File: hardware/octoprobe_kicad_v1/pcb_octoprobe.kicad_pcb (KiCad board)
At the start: 2 copper layers, 100 x 160 mm, 624 parts, among them J1001 Conn_01x02_Socket, J1002 Conn_01x02_Socket, J1003 Conn_01x02_Pin, J101 Conn_01x20, J102 Conn_01x20, J103 Conn_01x20, J201 USB_C_Receptacle_USB2.0, J301 Conn_01x02_Socket, J302 Conn_01x02_Socket, J303 Conn_01x02_Pin, J401 Conn_01x02_Socket, J402 Conn_01x02_Socket, J403 Conn_01x02_Pin, J501 Conn_01x02_Socket, J502 Conn_01x02_Socket, J503 Conn_01x02_Pin, J601 Conn_01x02_Socket, J602 Conn_01x02_Socket, J603 Conn_01x02_Pin, J701 Conn_01x02_Socket, J702 Conn_01x02_Socket, J703 Conn_01x02_Pin, J801 Conn_01x02_Socket, J802 Conn_01x02_Socket, J803 Conn_01x02_Pin, J901 Conn_01x02_Socket, J902 Conn_01x02_Socket, J903 Conn_01x02_Pin, SW201 SW_MEC_5E, U1001 GAQY221S, U201 RP2040, U202 AMS1117-3.3, U203 W25Q128JVS, U301 GAQY221S, U401 GAQY221S, U701 GAQY221S, U901 GAQY221S, Y201 Crystal_GND24_Small

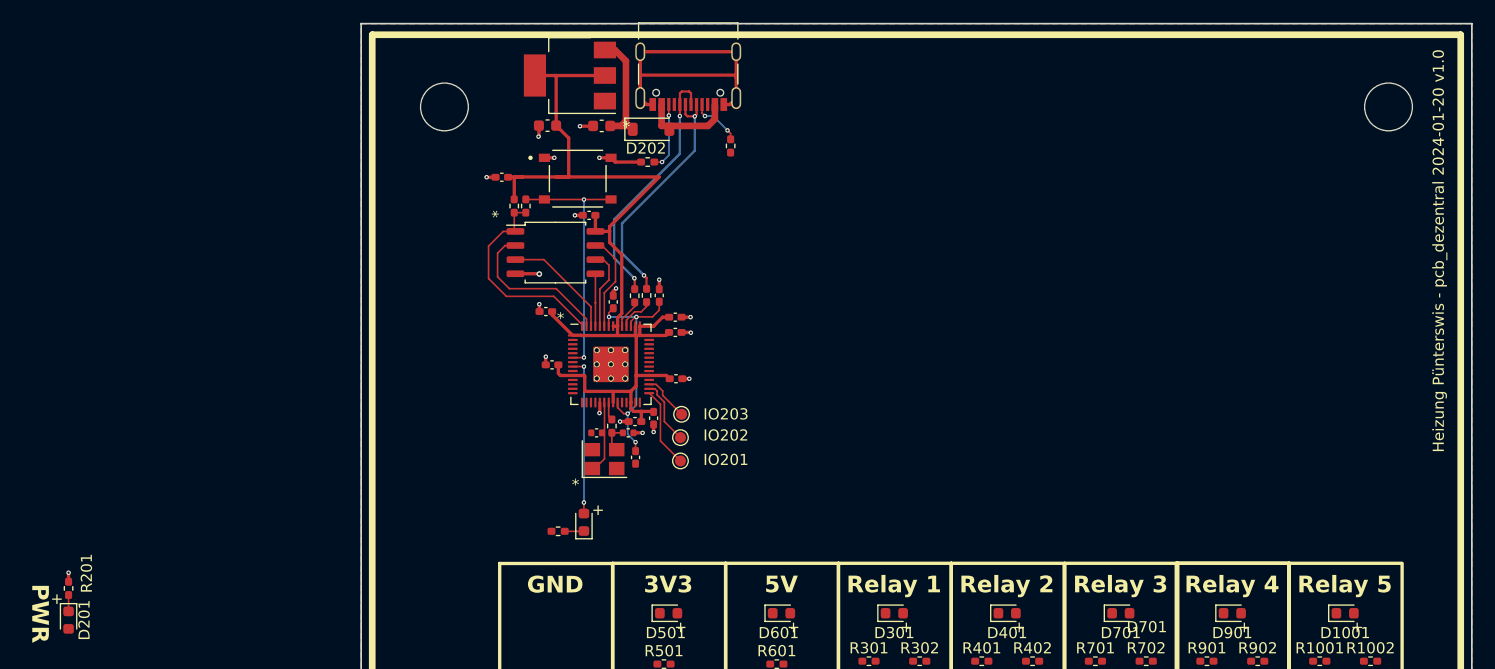
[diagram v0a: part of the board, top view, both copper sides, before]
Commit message: update sheet names
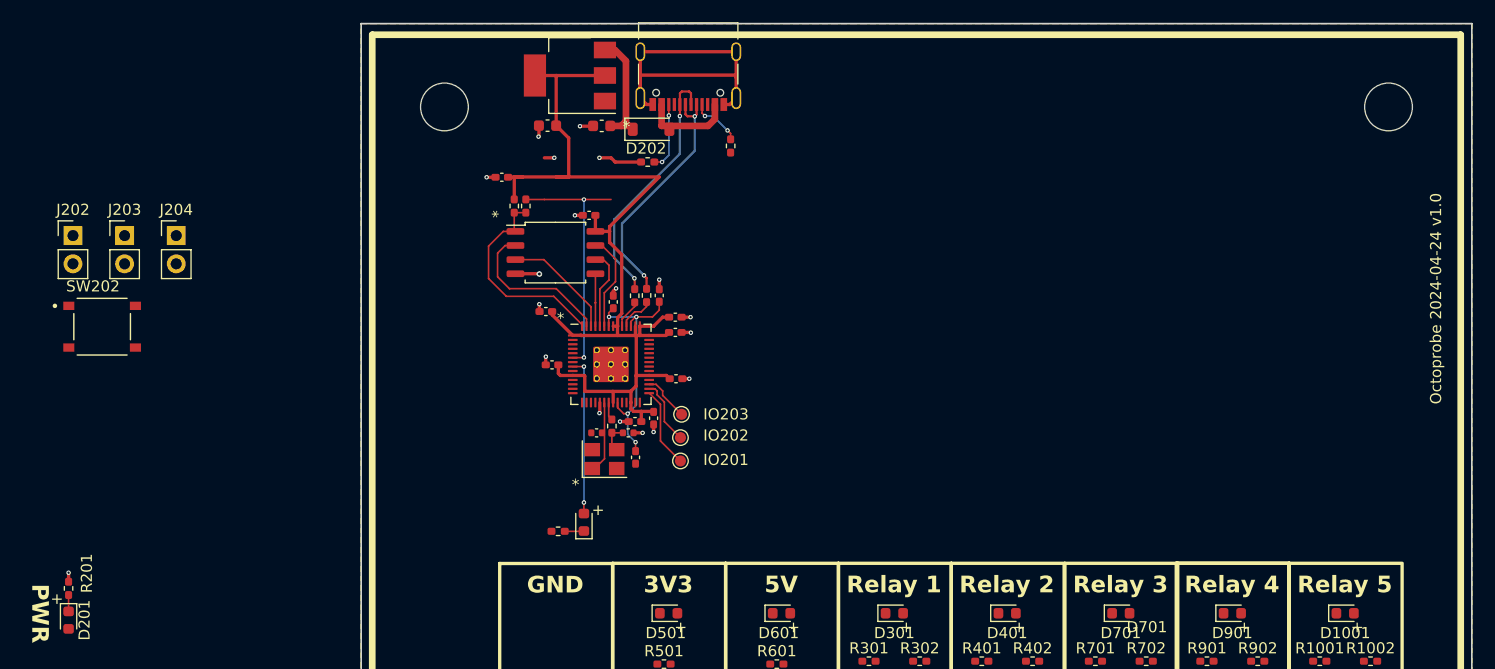
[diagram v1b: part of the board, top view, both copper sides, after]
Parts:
- removed SW201: SW_MEC_5E, 00_project_library:SW_TS-1187A-B-A-B
- added J202: BOOT cap enable, Connector_PinHeader_2.54mm:PinHeader_1x02_P2.54mm_Vertical, F.Cu at (48.1, 51.6)
- added J203: BOOT Button, Connector_PinHeader_2.54mm:PinHeader_1x02_P2.54mm_Vertical, F.Cu at (52.7, 51.6)
- added J204: BOOT cap 2, Connector_PinHeader_2.54mm:PinHeader_1x02_P2.54mm_Vertical, F.Cu at (57.4, 51.6)
- added SW202: RESET, 00_project_library:SW_TS-1187A-B-A-B, F.Cu at (50.7, 59.8)
- R1002, R302, R402, R702, R902: value 10K -> 4k2
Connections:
- U201 pad 26: +3V3 -> Net-(U201-RUN)

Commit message: Breakout Board
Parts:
- removed the REF** at (79.1, 129.0)
- removed REF**1, REF**10, REF**100, REF**101, REF**102, REF**103, REF**104, REF**105, REF**106, REF**107, REF**108, REF**109, REF**11, REF**110, REF**111, REF**112, REF**113, REF**114, REF**115, REF**116, REF**117, REF**118, REF**119, REF**12, REF**120, REF**121, REF**122, REF**123, REF**124, REF**125, REF**126, REF**127, REF**128, REF**129, REF**13, REF**130, REF**131, REF**132, REF**133, REF**134, REF**135, REF**136, REF**137, REF**138, REF**139, REF**14, REF**140, REF**141, REF**142, REF**143, REF**144, REF**145, REF**146, REF**147, REF**148, REF**149, REF**15, REF**150, REF**151, REF**152, REF**153, REF**154, REF**155, REF**156, REF**157, REF**158, REF**159, REF**16, REF**160, REF**161, REF**162, REF**163, REF**164, REF**165, REF**166, REF**167, REF**168, REF**169, REF**17, REF**170, REF**171, REF**172, REF**173, REF**174, REF**175, REF**176, REF**177, REF**178, REF**179, REF**18, REF**180, REF**181, REF**182, REF**183, REF**184, REF**185, REF**186, REF**187, REF**188, REF**189, REF**19, REF**190, REF**191, REF**192, REF**193, REF**194, REF**195, REF**196, REF**197, REF**198, REF**199, REF**2, REF**20, REF**200, REF**201, REF**202, REF**203, REF**204, REF**205, REF**206, REF**207, REF**208, REF**209, REF**21, REF**210, REF**211, REF**212, REF**213, REF**214, REF**215, REF**216, REF**217, REF**218, REF**219, REF**22, REF**220, REF**221, REF**222, REF**223, REF**224, REF**225, REF**226, REF**227, REF**228, REF**229, REF**23, REF**230, REF**231, REF**232, REF**233, REF**234, REF**235, REF**236, REF**237, REF**238, REF**239, REF**24, REF**240, REF**241, REF**242, REF**243, REF**244, REF**245, REF**246, REF**247, REF**248, REF**249, REF**25, REF**250, REF**251, REF**252, REF**253, REF**254, REF**255, REF**256, REF**257, REF**258, REF**259, REF**26, REF**260, REF**261, REF**262, REF**263, REF**264, REF**265, REF**266, REF**267, REF**268, REF**269, REF**27, REF**270, REF**271, REF**272, REF**273, REF**274, REF**275, REF**276, REF**277, REF**278, REF**279, REF**28, REF**280, REF**281, REF**282, REF**283, REF**284, REF**285, REF**286, REF**287, REF**288, REF**289, REF**29, REF**290, REF**291, REF**292, REF**293, REF**294, REF**295, REF**296, REF**297, REF**298, REF**299, REF**3, REF**30, REF**300, REF**301, REF**302, REF**303, REF**304, REF**305, REF**306, REF**307, REF**308, REF**309, REF**31, REF**310, REF**311, REF**312, REF**313, REF**314, REF**315, REF**316, REF**317, REF**318, REF**319, REF**32, REF**320, REF**321, REF**322, REF**323, REF**324, REF**325, REF**326, REF**327, REF**328, REF**329, REF**33, REF**330, REF**331, REF**332, REF**333, REF**334, REF**335, REF**336, REF**337, REF**338, REF**339, REF**34, REF**340, REF**341, REF**342, REF**343, REF**344, REF**345, REF**346, REF**347, REF**348, REF**349, REF**35, REF**350, REF**351, REF**352, REF**353, REF**354, REF**355, REF**356, REF**357, REF**358, REF**359, REF**36, REF**360, REF**361, REF**362, REF**363, REF**364, REF**365, REF**366, REF**367, REF**368, REF**369, REF**37, REF**370, REF**371, REF**372, REF**373, REF**374, REF**375, REF**376, REF**377, REF**378, REF**379, REF**38, REF**380, REF**381, REF**382, REF**383, REF**384, REF**385, REF**386, REF**387, REF**388, REF**389, REF**39, REF**390, REF**391, REF**392, REF**393, REF**394, REF**395, REF**396, REF**397, REF**398, REF**399, REF**4, REF**40, REF**400, REF**401, REF**402, REF**403, REF**404, REF**405, REF**406, REF**407, REF**408, REF**409, REF**41, REF**410, REF**411, REF**412, REF**413, REF**414, REF**415, REF**416, REF**417, REF**418, REF**419, REF**42, REF**420, REF**421, REF**422, REF**423, REF**424, REF**425, REF**426, REF**427, REF**428, REF**429, REF**43, REF**430, REF**431, REF**432, REF**433, REF**434, REF**435, REF**436, REF**437, REF**438, REF**439, REF**44, REF**440, REF**441, REF**442, REF**443, REF**444, REF**445, REF**446, REF**447, REF**448, REF**449, REF**45, REF**450, REF**451, REF**452, REF**453, REF**454, REF**455, REF**456, REF**457, REF**458, REF**459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: TestPoint_THTPad_D2.0mm_Drill1.0mm, TestPoint:TestPoint_THTPad_D2.0mm_Drill1.0mm
- added BP101: octoprobe_prototype_board, 00_project_library:octoprobe_breakout_PB, F.Cu at (79.1, 129.0)
- added BP102: octoprobe_prototype_board, 00_project_library:octoprobe_breakout_PB, F.Cu at (81.6, 129.0)
- added BP103: octoprobe_prototype_board, 00_project_library:octoprobe_breakout_PB, F.Cu at (84.2, 129.0)
- added BP104: octoprobe_prototype_board, 00_project_library:octoprobe_breakout_PB, F.Cu at (86.7, 129.0)
- added BP105: octoprobe_prototype_board, 00_project_library:octoprobe_breakout_PB, F.Cu at (89.2, 129.0)
- added BP106: octoprobe_prototype_board, 00_project_library:octoprobe_breakout_PB, F.Cu at (91.8, 129.0)
- added BP107: octoprobe_prototype_board, 00_project_library:octoprobe_breakout_PB, F.Cu at (94.3, 129.0)
- added BP108: octoprobe_prototype_board, 00_project_library:octoprobe_breakout_PB, F.Cu at (96.9, 129.0)
- added BP109: octoprobe_prototype_board, 00_project_library:octoprobe_breakout_PB, F.Cu at (99.4, 129.0)
- added BP110: octoprobe_prototype_board, 00_project_library:octoprobe_breakout_PB, F.Cu at (101.9, 129.0)
- added BP111: octoprobe_prototype_board, 00_project_library:octoprobe_breakout_PB, F.Cu at (104.5, 129.0)
- added BP112: octoprobe_prototype_board, 00_project_library:octoprobe_breakout_PB, F.Cu at (107.0, 129.0)
- added BP113: octoprobe_prototype_board, 00_project_library:octoprobe_breakout_PB, F.Cu at (109.6, 129.0)
- added BP114: octoprobe_prototype_board, 00_project_library:octoprobe_breakout_PB, F.Cu at (112.1, 129.0)
- added BP115: octoprobe_prototype_board, 00_project_library:octoprobe_breakout_PB, F.Cu at (114.6, 129.0)
- added BP116: octoprobe_prototype_board, 00_project_library:octoprobe_breakout_PB, F.Cu at (117.2, 129.0)
- added BP117: octoprobe_prototype_board, 00_project_library:octoprobe_breakout_PB, F.Cu at (119.7, 129.0)
- added BP118: octoprobe_prototype_board, 00_project_library:octoprobe_breakout_PB, F.Cu at (122.3, 129.0)
- added BP119: octoprobe_prototype_board, 00_project_library:octoprobe_breakout_PB, F.Cu at (124.8, 129.0)
- added BP120: octoprobe_prototype_board, 00_project_library:octoprobe_breakout_PB, F.Cu at (127.3, 129.0)
- added BP121: octoprobe_prototype_board, 00_project_library:octoprobe_breakout_PB, F.Cu at (129.9, 129.0)
- added BP122: octoprobe_prototype_board, 00_project_library:octoprobe_breakout_PB, F.Cu at (132.4, 129.0)
- added BP123: octoprobe_prototype_board, 00_project_library:octoprobe_breakout_PB, F.Cu at (135.0, 129.0)
- added BP124: octoprobe_prototype_board, 00_project_library:octoprobe_breakout_PB, F.Cu at (137.5, 129.0)
- added BP125: octoprobe_prototype_board, 00_project_library:octoprobe_breakout_PB, F.Cu at (140.0, 129.0)
- added BP126: octoprobe_prototype_board, 00_project_library:octoprobe_breakout_PB, F.Cu at (142.6, 129.0)
- added BP127: octoprobe_prototype_board, 00_project_library:octoprobe_breakout_PB, F.Cu at (79.1, 131.6)
- added BP128: octoprobe_prototype_board, 00_project_library:octoprobe_breakout_PB, F.Cu at (81.6, 131.6)
- added BP129: octoprobe_prototype_board, 00_project_library:octoprobe_breakout_PB, F.Cu at (84.2, 131.6)
- added BP130: octoprobe_prototype_board, 00_project_library:octoprobe_breakout_PB, F.Cu at (86.7, 131.6)
- added BP131: octoprobe_prototype_board, 00_project_library:octoprobe_breakout_PB, F.Cu at (89.2, 131.6)
- added BP132: octoprobe_prototype_board, 00_project_library:octoprobe_breakout_PB, F.Cu at (91.8, 131.6)
- added BP133: octoprobe_prototype_board, 00_project_library:octoprobe_breakout_PB, F.Cu at (94.3, 131.6)
- added BP134: octoprobe_prototype_board, 00_project_library:octoprobe_breakout_PB, F.Cu at (96.9, 131.6)
- added BP135: octoprobe_prototype_board, 00_project_library:octoprobe_breakout_PB, F.Cu at (99.4, 131.6)
- added BP136: octoprobe_prototype_board, 00_project_library:octoprobe_breakout_PB, F.Cu at (101.9, 131.6)
- added BP137: octoprobe_prototype_board, 00_project_library:octoprobe_breakout_PB, F.Cu at (104.5, 131.6)
- added BP138: octoprobe_prototype_board, 00_project_library:octoprobe_breakout_PB, F.Cu at (107.0, 131.6)
- added BP139: octoprobe_prototype_board, 00_project_library:octoprobe_breakout_PB, F.Cu at (109.6, 131.6)
- added BP140: octoprobe_prototype_board, 00_project_library:octoprobe_breakout_PB, F.Cu at (112.1, 131.6)
- added BP141: octoprobe_prototype_board, 00_project_library:octoprobe_breakout_PB, F.Cu at (114.6, 131.6)
- added BP142: octoprobe_prototype_board, 00_project_library:octoprobe_breakout_PB, F.Cu at (117.2, 131.6)
- added BP143: octoprobe_prototype_board, 00_project_library:octoprobe_breakout_PB, F.Cu at (119.7, 131.6)
- added BP144: octoprobe_prototype_board, 00_project_library:octoprobe_breakout_PB, F.Cu at (122.3, 131.6)
- added BP145: octoprobe_prototype_board, 00_project_library:octoprobe_breakout_PB, F.Cu at (124.8, 131.6)
- added BP146: octoprobe_prototype_board, 00_project_library:octoprobe_breakout_PB, F.Cu at (127.3, 131.6)
- added BP147: octoprobe_prototype_board, 00_project_library:octoprobe_breakout_PB, F.Cu at (129.9, 131.6)
- added BP148: octoprobe_prototype_board, 00_project_library:octoprobe_breakout_PB, F.Cu at (132.4, 131.6)
- added BP149: octoprobe_prototype_board, 00_project_library:octoprobe_breakout_PB, F.Cu at (135.0, 131.6)
- added BP150: octoprobe_prototype_board, 00_project_library:octoprobe_breakout_PB, F.Cu at (137.5, 131.6)
- added BP151: octoprobe_prototype_board, 00_project_library:octoprobe_breakout_PB, F.Cu at (140.0, 131.6)
- added BP152: octoprobe_prototype_board, 00_project_library:octoprobe_breakout_PB, F.Cu at (142.6, 131.6)
- added BP153: octoprobe_prototype_board, 00_project_library:octoprobe_breakout_PB, F.Cu at (79.1, 134.1)
- added BP154: octoprobe_prototype_board, 00_project_library:octoprobe_breakout_PB, F.Cu at (81.6, 134.1)
- added BP155: octoprobe_prototype_board, 00_project_library:octoprobe_breakout_PB, F.Cu at (84.2, 134.1)
- added BP156: octoprobe_prototype_board, 00_project_library:octoprobe_breakout_PB, F.Cu at (86.7, 134.1)
- added BP157: octoprobe_prototype_board, 00_project_library:octoprobe_breakout_PB, F.Cu at (89.2, 134.1)
- added BP158: octoprobe_prototype_board, 00_project_library:octoprobe_breakout_PB, F.Cu at (91.8, 134.1)
- added BP159: octoprobe_prototype_board, 00_project_library:octoprobe_breakout_PB, F.Cu at (94.3, 134.1)
- added BP160: octoprobe_prototype_board, 00_project_library:octoprobe_breakout_PB, F.Cu at (96.9, 134.1)
- added BP161: octoprobe_prototype_board, 00_project_library:octoprobe_breakout_PB, F.Cu at (99.4, 134.1)
- added BP162: octoprobe_prototype_board, 00_project_library:octoprobe_breakout_PB, F.Cu at (101.9, 134.1)
- added BP163: octoprobe_prototype_board, 00_project_library:octoprobe_breakout_PB, F.Cu at (104.5, 134.1)
- added BP164: octoprobe_prototype_board, 00_project_library:octoprobe_breakout_PB, F.Cu at (107.0, 134.1)
- added BP165: octoprobe_prototype_board, 00_project_library:octoprobe_breakout_PB, F.Cu at (109.6, 134.1)
- added BP166: octoprobe_prototype_board, 00_project_library:octoprobe_breakout_PB, F.Cu at (112.1, 134.1)
- added BP167: octoprobe_prototype_board, 00_project_library:octoprobe_breakout_PB, F.Cu at (114.6, 134.1)
- added BP168: octoprobe_prototype_board, 00_project_library:octoprobe_breakout_PB, F.Cu at (117.2, 134.1)
- added BP169: octoprobe_prototype_board, 00_project_library:octoprobe_breakout_PB, F.Cu at (119.7, 134.1)
- added BP170: octoprobe_prototype_board, 00_project_library:octoprobe_breakout_PB, F.Cu at (122.3, 134.1)
- added BP171: octoprobe_prototype_board, 00_project_library:octoprobe_breakout_PB, F.Cu at (124.8, 134.1)
- added BP172: octoprobe_prototype_board, 00_project_library:octoprobe_breakout_PB, F.Cu at (127.3, 134.1)
- added BP173: octoprobe_prototype_board, 00_project_library:octoprobe_breakout_PB, F.Cu at (129.9, 134.1)
- added BP174: octoprobe_prototype_board, 00_project_library:octoprobe_breakout_PB, F.Cu at (132.4, 134.1)
- added BP175: octoprobe_prototype_board, 00_project_library:octoprobe_breakout_PB, F.Cu at (135.0, 134.1)
- added BP176: octoprobe_prototype_board, 00_project_library:octoprobe_breakout_PB, F.Cu at (137.5, 134.1)
- added BP177: octoprobe_prototype_board, 00_project_library:octoprobe_breakout_PB, F.Cu at (140.0, 134.1)
- added BP178: octoprobe_prototype_board, 00_project_library:octoprobe_breakout_PB, F.Cu at (142.6, 134.1)
- added BP179: octoprobe_prototype_board, 00_project_library:octoprobe_breakout_PB, F.Cu at (79.1, 136.6)
- added BP180: octoprobe_prototype_board, 00_project_library:octoprobe_breakout_PB, F.Cu at (81.6, 136.6)
- added BP181: octoprobe_prototype_board, 00_project_library:octoprobe_breakout_PB, F.Cu at (84.2, 136.6)
- added BP182: octoprobe_prototype_board, 00_project_library:octoprobe_breakout_PB, F.Cu at (86.7, 136.6)
- added BP183: octoprobe_prototype_board, 00_project_library:octoprobe_breakout_PB, F.Cu at (89.2, 136.6)
- added BP184: octoprobe_prototype_board, 00_project_library:octoprobe_breakout_PB, F.Cu at (91.8, 136.6)
- added BP185: octoprobe_prototype_board, 00_project_library:octoprobe_breakout_PB, F.Cu at (94.3, 136.6)
- added BP186: octoprobe_prototype_board, 00_project_library:octoprobe_breakout_PB, F.Cu at (96.9, 136.6)
- added BP187: octoprobe_prototype_board, 00_project_library:octoprobe_breakout_PB, F.Cu at (99.4, 136.6)
- added BP188: octoprobe_prototype_board, 00_project_library:octoprobe_breakout_PB, F.Cu at (101.9, 136.6)
- added BP189: octoprobe_prototype_board, 00_project_library:octoprobe_breakout_PB, F.Cu at (104.5, 136.6)
- added BP190: octoprobe_prototype_board, 00_project_library:octoprobe_breakout_PB, F.Cu at (107.0, 136.6)
- added BP191: octoprobe_prototype_board, 00_project_library:octoprobe_breakout_PB, F.Cu at (109.6, 136.6)
- added BP192: octoprobe_prototype_board, 00_project_library:octoprobe_breakout_PB, F.Cu at (112.1, 136.6)
- added BP193: octoprobe_prototype_board, 00_project_library:octoprobe_breakout_PB, F.Cu at (114.6, 136.6)
- added BP194: octoprobe_prototype_board, 00_project_library:octoprobe_breakout_PB, F.Cu at (117.2, 136.6)
- added BP195: octoprobe_prototype_board, 00_project_library:octoprobe_breakout_PB, F.Cu at (119.7, 136.6)
- added BP196: octoprobe_prototype_board, 00_project_library:octoprobe_breakout_PB, F.Cu at (122.3, 136.6)
- added BP197: octoprobe_prototype_board, 00_project_library:octoprobe_breakout_PB, F.Cu at (124.8, 136.6)
- added BP198: octoprobe_prototype_board, 00_project_library:octoprobe_breakout_PB, F.Cu at (127.3, 136.6)
- added BP199: octoprobe_prototype_board, 00_project_library:octoprobe_breakout_PB, F.Cu at (129.9, 136.6)
- added BP200: octoprobe_prototype_board, 00_project_library:octoprobe_breakout_PB, F.Cu at (132.4, 136.6)
- added BP201: octoprobe_prototype_board, 00_project_library:octoprobe_breakout_PB, F.Cu at (135.0, 136.6)
- added BP202: octoprobe_prototype_board, 00_project_library:octoprobe_breakout_PB, F.Cu at (137.5, 136.6)
- added BP203: octoprobe_prototype_board, 00_project_library:octoprobe_breakout_PB, F.Cu at (140.0, 136.6)
- added BP204: octoprobe_prototype_board, 00_project_library:octoprobe_breakout_PB, F.Cu at (142.6, 136.6)
- added BP205: octoprobe_prototype_board, 00_project_library:octoprobe_breakout_PB, F.Cu at (79.1, 139.2)
- added BP206: octoprobe_prototype_board, 00_project_library:octoprobe_breakout_PB, F.Cu at (81.6, 139.2)
- added BP207: octoprobe_prototype_board, 00_project_library:octoprobe_breakout_PB, F.Cu at (84.2, 139.2)
- added BP208: octoprobe_prototype_board, 00_project_library:octoprobe_breakout_PB, F.Cu at (86.7, 139.2)
- added BP209: octoprobe_prototype_board, 00_project_library:octoprobe_breakout_PB, F.Cu at (89.2, 139.2)
- added BP210: octoprobe_prototype_board, 00_project_library:octoprobe_breakout_PB, F.Cu at (91.8, 139.2)
- added BP211: octoprobe_prototype_board, 00_project_library:octoprobe_breakout_PB, F.Cu at (94.3, 139.2)
- added BP212: octoprobe_prototype_board, 00_project_library:octoprobe_breakout_PB, F.Cu at (96.9, 139.2)
- added BP213: octoprobe_prototype_board, 00_project_library:octoprobe_breakout_PB, F.Cu at (99.4, 139.2)
- added BP214: octoprobe_prototype_board, 00_project_library:octoprobe_breakout_PB, F.Cu at (101.9, 139.2)
- added BP215: octoprobe_prototype_board, 00_project_library:octoprobe_breakout_PB, F.Cu at (104.5, 139.2)
- added BP216: octoprobe_prototype_board, 00_project_library:octoprobe_breakout_PB, F.Cu at (107.0, 139.2)
- added BP217: octoprobe_prototype_board, 00_project_library:octoprobe_breakout_PB, F.Cu at (109.6, 139.2)
- added BP218: octoprobe_prototype_board, 00_project_library:octoprobe_breakout_PB, F.Cu at (112.1, 139.2)
- added BP219: octoprobe_prototype_board, 00_project_library:octoprobe_breakout_PB, F.Cu at (114.6, 139.2)
- added BP220: octoprobe_prototype_board, 00_project_library:octoprobe_breakout_PB, F.Cu at (117.2, 139.2)
- added BP221: octoprobe_prototype_board, 00_project_library:octoprobe_breakout_PB, F.Cu at (119.7, 139.2)
- added BP222: octoprobe_prototype_board, 00_project_library:octoprobe_breakout_PB, F.Cu at (122.3, 139.2)
- added BP223: octoprobe_prototype_board, 00_project_library:octoprobe_breakout_PB, F.Cu at (124.8, 139.2)
- added BP224: octoprobe_prototype_board, 00_project_library:octoprobe_breakout_PB, F.Cu at (127.3, 139.2)
- added BP225: octoprobe_prototype_board, 00_project_library:octoprobe_breakout_PB, F.Cu at (129.9, 139.2)
- added BP226: octoprobe_prototype_board, 00_project_library:octoprobe_breakout_PB, F.Cu at (132.4, 139.2)
- added BP227: octoprobe_prototype_board, 00_project_library:octoprobe_breakout_PB, F.Cu at (135.0, 139.2)
- added BP228: octoprobe_prototype_board, 00_project_library:octoprobe_breakout_PB, F.Cu at (137.5, 139.2)
- added BP229: octoprobe_prototype_board, 00_project_library:octoprobe_breakout_PB, F.Cu at (140.0, 139.2)
- added BP230: octoprobe_prototype_board, 00_project_library:octoprobe_breakout_PB, F.Cu at (142.6, 139.2)
- added BP231: octoprobe_prototype_board, 00_project_library:octoprobe_breakout_PB, F.Cu at (79.1, 141.7)
- added BP232: octoprobe_prototype_board, 00_project_library:octoprobe_breakout_PB, F.Cu at (81.6, 141.7)
- added BP233: octoprobe_prototype_board, 00_project_library:octoprobe_breakout_PB, F.Cu at (84.2, 141.7)
- added BP234: octoprobe_prototype_board, 00_project_library:octoprobe_breakout_PB, F.Cu at (86.7, 141.7)
- added BP235: octoprobe_prototype_board, 00_project_library:octoprobe_breakout_PB, F.Cu at (89.2, 141.7)
- added BP236: octoprobe_prototype_board, 00_project_library:octoprobe_breakout_PB, F.Cu at (91.8, 141.7)
- added BP237: octoprobe_prototype_board, 00_project_library:octoprobe_breakout_PB, F.Cu at (94.3, 141.7)
- added BP238: octoprobe_prototype_board, 00_project_library:octoprobe_breakout_PB, F.Cu at (96.9, 141.7)
- added BP239: octoprobe_prototype_board, 00_project_library:octoprobe_breakout_PB, F.Cu at (99.4, 141.7)
- added BP240: octoprobe_prototype_board, 00_project_library:octoprobe_breakout_PB, F.Cu at (101.9, 141.7)
- added BP241: octoprobe_prototype_board, 00_project_library:octoprobe_breakout_PB, F.Cu at (104.5, 141.7)
- added BP242: octoprobe_prototype_board, 00_project_library:octoprobe_breakout_PB, F.Cu at (107.0, 141.7)
- added BP243: octoprobe_prototype_board, 00_project_library:octoprobe_breakout_PB, F.Cu at (109.6, 141.7)
- added BP244: octoprobe_prototype_board, 00_project_library:octoprobe_breakout_PB, F.Cu at (112.1, 141.7)
- added BP245: octoprobe_prototype_board, 00_project_library:octoprobe_breakout_PB, F.Cu at (114.6, 141.7)
- added BP246: octoprobe_prototype_board, 00_project_library:octoprobe_breakout_PB, F.Cu at (117.2, 141.7)
- added BP247: octoprobe_prototype_board, 00_project_library:octoprobe_breakout_PB, F.Cu at (119.7, 141.7)
- added BP248: octoprobe_prototype_board, 00_project_library:octoprobe_breakout_PB, F.Cu at (122.3, 141.7)
- added BP249: octoprobe_prototype_board, 00_project_library:octoprobe_breakout_PB, F.Cu at (124.8, 141.7)
- added BP250: octoprobe_prototype_board, 00_project_library:octoprobe_breakout_PB, F.Cu at (127.3, 141.7)
- added BP251: octoprobe_prototype_board, 00_project_library:octoprobe_breakout_PB, F.Cu at (129.9, 141.7)
- added BP252: octoprobe_prototype_board, 00_project_library:octoprobe_breakout_PB, F.Cu at (132.4, 141.7)
- added BP253: octoprobe_prototype_board, 00_project_library:octoprobe_breakout_PB, F.Cu at (135.0, 141.7)
- added BP254: octoprobe_prototype_board, 00_project_library:octoprobe_breakout_PB, F.Cu at (137.5, 141.7)
- added BP255: octoprobe_prototype_board, 00_project_library:octoprobe_breakout_PB, F.Cu at (140.0, 141.7)
- added BP256: octoprobe_prototype_board, 00_project_library:octoprobe_breakout_PB, F.Cu at (142.6, 141.7)
- added BP257: octoprobe_prototype_board, 00_project_library:octoprobe_breakout_PB, F.Cu at (79.1, 144.3)
- added BP258: octoprobe_prototype_board, 00_project_library:octoprobe_breakout_PB, F.Cu at (81.6, 144.3)
- added BP259: octoprobe_prototype_board, 00_project_library:octoprobe_breakout_PB, F.Cu at (84.2, 144.3)
- added BP260: octoprobe_prototype_board, 00_project_library:octoprobe_breakout_PB, F.Cu at (86.7, 144.3)
- added BP261: octoprobe_prototype_board, 00_project_library:octoprobe_breakout_PB, F.Cu at (89.2, 144.3)
- added BP262: octoprobe_prototype_board, 00_project_library:octoprobe_breakout_PB, F.Cu at (91.8, 144.3)
- added BP263: octoprobe_prototype_board, 00_project_library:octoprobe_breakout_PB, F.Cu at (94.3, 144.3)
- added BP264: octoprobe_prototype_board, 00_project_library:octoprobe_breakout_PB, F.Cu at (96.9, 144.3)
- added BP265: octoprobe_prototype_board, 00_project_library:octoprobe_breakout_PB, F.Cu at (99.4, 144.3)
- added BP266: octoprobe_prototype_board, 00_project_library:octoprobe_breakout_PB, F.Cu at (101.9, 144.3)
- added BP267: octoprobe_prototype_board, 00_project_library:octoprobe_breakout_PB, F.Cu at (104.5, 144.3)
- added BP268: octoprobe_prototype_board, 00_project_library:octoprobe_breakout_PB, F.Cu at (107.0, 144.3)
- added BP269: octoprobe_prototype_board, 00_project_library:octoprobe_breakout_PB, F.Cu at (109.6, 144.3)
- added BP270: octoprobe_prototype_board, 00_project_library:octoprobe_breakout_PB, F.Cu at (112.1, 144.3)
- added BP271: octoprobe_prototype_board, 00_project_library:octoprobe_breakout_PB, F.Cu at (114.6, 144.3)
- added BP272: octoprobe_prototype_board, 00_project_library:octoprobe_breakout_PB, F.Cu at (117.2, 144.3)
- added BP273: octoprobe_prototype_board, 00_project_library:octoprobe_breakout_PB, F.Cu at (119.7, 144.3)
- added BP274: octoprobe_prototype_board, 00_project_library:octoprobe_breakout_PB, F.Cu at (122.3, 144.3)
- added BP275: octoprobe_prototype_board, 00_project_library:octoprobe_breakout_PB, F.Cu at (124.8, 144.3)
- added BP276: octoprobe_prototype_board, 00_project_library:octoprobe_breakout_PB, F.Cu at (127.3, 144.3)
- added BP277: octoprobe_prototype_board, 00_project_library:octoprobe_breakout_PB, F.Cu at (129.9, 144.3)
- added BP278: octoprobe_prototype_board, 00_project_library:octoprobe_breakout_PB, F.Cu at (132.4, 144.3)
- added BP279: octoprobe_prototype_board, 00_project_library:octoprobe_breakout_PB, F.Cu at (135.0, 144.3)
- added BP280: octoprobe_prototype_board, 00_project_library:octoprobe_breakout_PB, F.Cu at (137.5, 144.3)
- added BP281: octoprobe_prototype_board, 00_project_library:octoprobe_breakout_PB, F.Cu at (140.0, 144.3)
- added BP282: octoprobe_prototype_board, 00_project_library:octoprobe_breakout_PB, F.Cu at (142.6, 144.3)
- added BP283: octoprobe_prototype_board, 00_project_library:octoprobe_breakout_PB, F.Cu at (79.1, 146.8)
- added BP284: octoprobe_prototype_board, 00_project_library:octoprobe_breakout_PB, F.Cu at (81.6, 146.8)
- added BP285: octoprobe_prototype_board, 00_project_library:octoprobe_breakout_PB, F.Cu at (84.2, 146.8)
- added BP286: octoprobe_prototype_board, 00_project_library:octoprobe_breakout_PB, F.Cu at (86.7, 146.8)
- added BP287: octoprobe_prototype_board, 00_project_library:octoprobe_breakout_PB, F.Cu at (89.2, 146.8)
- added BP288: octoprobe_prototype_board, 00_project_library:octoprobe_breakout_PB, F.Cu at (91.8, 146.8)
- added BP289: octoprobe_prototype_board, 00_project_library:octoprobe_breakout_PB, F.Cu at (94.3, 146.8)
- added BP290: octoprobe_prototype_board, 00_project_library:octoprobe_breakout_PB, F.Cu at (96.9, 146.8)
- added BP291: octoprobe_prototype_board, 00_project_library:octoprobe_breakout_PB, F.Cu at (99.4, 146.8)
- added BP292: octoprobe_prototype_board, 00_project_library:octoprobe_breakout_PB, F.Cu at (101.9, 146.8)
- added BP293: octoprobe_prototype_board, 00_project_library:octoprobe_breakout_PB, F.Cu at (104.5, 146.8)
- added BP294: octoprobe_prototype_board, 00_project_library:octoprobe_breakout_PB, F.Cu at (107.0, 146.8)
- added BP295: octoprobe_prototype_board, 00_project_library:octoprobe_breakout_PB, F.Cu at (109.6, 146.8)
- added BP296: octoprobe_prototype_board, 00_project_library:octoprobe_breakout_PB, F.Cu at (112.1, 146.8)
- added BP297: octoprobe_prototype_board, 00_project_library:octoprobe_breakout_PB, F.Cu at (114.6, 146.8)
- added BP298: octoprobe_prototype_board, 00_project_library:octoprobe_breakout_PB, F.Cu at (117.2, 146.8)
- added BP299: octoprobe_prototype_board, 00_project_library:octoprobe_breakout_PB, F.Cu at (119.7, 146.8)
- added BP300: octoprobe_prototype_board, 00_project_library:octoprobe_breakout_PB, F.Cu at (122.3, 146.8)
- added BP301: octoprobe_prototype_board, 00_project_library:octoprobe_breakout_PB, F.Cu at (124.8, 146.8)
- added BP302: octoprobe_prototype_board, 00_project_library:octoprobe_breakout_PB, F.Cu at (127.3, 146.8)
- added BP303: octoprobe_prototype_board, 00_project_library:octoprobe_breakout_PB, F.Cu at (129.9, 146.8)
- added BP304: octoprobe_prototype_board, 00_project_library:octoprobe_breakout_PB, F.Cu at (132.4, 146.8)
- added BP305: octoprobe_prototype_board, 00_project_library:octoprobe_breakout_PB, F.Cu at (135.0, 146.8)
- added BP306: octoprobe_prototype_board, 00_project_library:octoprobe_breakout_PB, F.Cu at (137.5, 146.8)
- added BP307: octoprobe_prototype_board, 00_project_library:octoprobe_breakout_PB, F.Cu at (140.0, 146.8)
- added BP308: octoprobe_prototype_board, 00_project_library:octoprobe_breakout_PB, F.Cu at (142.6, 146.8)
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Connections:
- J202 pad 2: button -> /cpu/QSPI_SS
- J203 pad 2: button -> Net-(J203-Pin_2)
- R206 pad 1: button -> Net-(J203-Pin_2)
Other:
- board text added: "GND"

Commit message: Mounting
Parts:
- removed REF** (x4): MountingHole_4.3mm_M4, MountingHole:MountingHole_4.3mm_M4
- added H101: octoprobe_MountingHole, MountingHole:MountingHole_3.2mm_M3_DIN965_Pad, F.Cu at (80.0, 38.5)
- added H102: octoprobe_MountingHole, MountingHole:MountingHole_3.2mm_M3_DIN965_Pad, F.Cu at (168.0, 38.5)
- added H103: octoprobe_MountingHole, MountingHole:MountingHole_3.2mm_M3_DIN965_Pad, F.Cu at (168.0, 186.5)
- added H104: octoprobe_MountingHole, MountingHole:MountingHole_3.2mm_M3_DIN965_Pad, F.Cu at (80.0, 186.5)
- renumbered BP616 to BP101, BP549 to BP101, BP438 to BP101, BP349 to BP101, BP209 to BP101, BP468 to BP101, BP330 to BP101, BP145 to BP101, BP181 to BP101, BP578 to BP101, BP505 to BP101, BP244 to BP101, BP335 to BP101, BP179 to BP101, BP374 to BP101, BP471 to BP101, BP457 to BP101, BP556 to BP101, BP533 to BP101, BP620 to BP101, BP286 to BP101, BP522 to BP101, BP557 to BP101, BP325 to BP101, BP323 to BP101, BP399 to BP101, BP237 to BP101, BP454 to BP101, BP239 to BP101, BP508 to BP101, BP111 to BP101, BP381 to BP101, BP184 to BP101, BP176 to BP101, BP221 to BP101, BP403 to BP101, BP333 to BP101, BP324 to BP101, BP271 to BP101, BP484 to BP101, BP276 to BP101, BP437 to BP101, BP120 to BP101, BP584 to BP101, BP310 to BP101, BP318 to BP101, BP605 to BP101, BP452 to BP101, BP600 to BP101, BP393 to BP101, BP510 to BP101, BP435 to BP101, BP226 to BP101, BP536 to BP101, BP401 to BP101, BP215 to BP101, BP606 to BP101, BP201 to BP101, BP554 to BP101, BP410 to BP101, BP487 to BP101, BP545 to BP101, BP225 to BP101, BP193 to BP101, BP253 to BP101, BP573 to BP101, BP285 to BP101, BP192 to BP101, BP448 to BP101, BP250 to BP101, BP477 to BP101, BP180 to BP101, BP581 to BP101, BP431 to BP101, BP103 to BP101, BP258 to BP101, BP601 to BP101, BP147 to BP101, BP361 to BP101, BP229 to BP101, BP156 to BP101, BP154 to BP101, BP353 to BP101, BP379 to BP101, BP433 to BP101, BP412 to BP101, BP142 to BP101, BP167 to BP101, BP305 to BP101, BP294 to BP101, BP183 to BP101, BP320 to BP101, BP587 to BP101, BP245 to BP101, BP372 to BP101, BP200 to BP101, BP255 to BP101, BP598 to BP101, BP413 to BP101, BP150 to BP101, BP133 to BP101, BP613 to BP101, BP493 to BP101, BP370 to BP101, BP306 to BP101, BP303 to BP101, BP213 to BP101, BP475 to BP101, BP321 to BP101, BP387 to BP101, BP523 to BP101, BP491 to BP101, BP196 to BP101, BP569 to BP101, BP165 to BP101, BP466 to BP101, BP509 to BP101, BP618 to BP101, BP344 to BP101, BP312 to BP101, BP396 to BP101, BP596 to BP101, BP261 to BP101, BP240 to BP101, BP497 to BP101, BP609 to BP101, BP265 to BP101, BP552 to BP101, BP402 to BP101, BP531 to BP101, BP336 to BP101, BP341 to BP101, BP227 to BP101, BP460 to BP101, BP550 to BP101, BP576 to BP101, BP346 to BP101, BP146 to BP101, BP338 to BP101, BP264 to BP101, BP249 to BP101, BP594 to BP101, BP365 to BP101, BP465 to BP101, BP368 to BP101, BP292 to BP101, BP478 to BP101, BP612 to BP101, BP496 to BP101, BP279 to BP101, BP315 to BP101, BP485 to BP101, BP441 to BP101, BP194 to BP101, BP153 to BP101, BP490 to BP101, BP503 to BP101, BP257 to BP101, BP499 to BP101, BP217 to BP101, BP546 to BP101, BP406 to BP101, BP205 to BP101, BP588 to BP101, BP208 to BP101, BP175 to BP101, BP235 to BP101, BP107 to BP101, BP382 to BP101, BP216 to BP101, BP483 to BP101, BP482 to BP101, BP416 to BP101, BP327 to BP101, BP506 to BP101, BP517 to BP101, BP189 to BP101, BP392 to BP101, BP281 to BP101, BP511 to BP101, BP619 to BP101, BP544 to BP101, BP291 to BP101, BP420 to BP101, BP223 to BP101, BP204 to BP101, BP110 to BP101, BP340 to BP101, BP367 to BP101, BP421 to BP101, BP394 to BP101, BP378 to BP101, BP274 to BP101, BP132 to BP101, BP520 to BP101, BP164 to BP101, BP131 to BP101, BP500 to BP101, BP307 to BP101, BP427 to BP101, BP228 to BP101, BP525 to BP101, BP113 to BP101, BP461 to BP101, BP445 to BP101, BP451 to BP101, BP242 to BP101, BP206 to BP101, BP127 to BP101, BP436 to BP101, BP319 to BP101, BP124 to BP101, BP362 to BP101, BP409 to BP101, BP530 to BP101, BP390 to BP101, BP570 to BP101, BP345 to BP101, BP214 to BP101, BP144 to BP101, BP158 to BP101, BP268 to BP101, BP207 to BP101, BP162 to BP101, BP233 to BP101, BP178 to BP101, BP287 to BP101, BP439 to BP101, BP152 to BP101, BP135 to BP101, BP296 to BP101, BP289 to BP101, BP424 to BP101, BP599 to BP101, BP430 to BP101, BP311 to BP101, BP247 to BP101, BP157 to BP101, BP583 to BP101, BP203 to BP101, BP579 to BP101, BP117 to BP101, BP125 to BP101, BP464 to BP101, BP602 to BP101, BP577 to BP101, BP432 to BP101, BP256 to BP101, BP121 to BP101, BP419 to BP101, BP404 to BP101, BP302 to BP101, BP197 to BP101, BP355 to BP101, BP138 to BP101, BP283 to BP101, BP469 to BP101, BP166 to BP101, BP479 to BP101, BP463 to BP101, BP275 to BP101, BP453 to BP101, BP555 to BP101, BP317 to BP101, BP220 to BP101, BP563 to BP101, BP534 to BP101, BP269 to BP101, BP551 to BP101, BP486 to BP101, BP580 to BP101, BP342 to BP101, BP343 to BP101, BP561 to BP101, BP241 to BP101, BP541 to BP101, BP384 to BP101, BP383 to BP101, BP334 to BP101, BP151 to BP101, BP352 to BP101, BP553 to BP101, BP299 to BP101, BP488 to BP101, BP123 to BP101, BP309 to BP101, BP492 to BP101, BP398 to BP101, BP119 to BP101, BP376 to BP101, BP246 to BP101, BP502 to BP101, BP290 to BP101, BP418 to BP101, BP537 to BP101, BP415 to BP101, BP316 to BP101, BP423 to BP101, BP231 to BP101, BP128 to BP101, BP608 to BP101, BP248 to BP101, BP385 to BP101, BP149 to BP101, BP174 to BP101, BP512 to BP101, BP514 to BP101, BP425 to BP101, BP547 to BP101, BP273 to BP101, BP115 to BP101, BP326 to BP101, BP277 to BP101, BP429 to BP101, BP106 to BP101, BP562 to BP101, BP314 to BP101, BP575 to BP101, BP472 to BP101, BP391 to BP101, BP400 to BP101, BP476 to BP101, BP371 to BP101, BP417 to BP101, BP130 to BP101, BP143 to BP101, BP585 to BP101, BP134 to BP101, BP263 to BP101, BP559 to BP101, BP219 to BP101, BP532 to BP101, BP473 to BP101, BP359 to BP101, BP139 to BP101, BP109 to BP101, BP408 to BP101, BP527 to BP101, BP515 to BP101, BP455 to BP101, BP560 to BP101, BP224 to BP101, BP540 to BP101, BP186 to BP101, BP526 to BP101, BP494 to BP101, BP363 to BP101, BP259 to BP101, BP428 to BP101, BP328 to BP101, BP529 to BP101, BP313 to BP101, BP270 to BP101, BP571 to BP101, BP543 to BP101, BP489 to BP101, BP565 to BP101, BP322 to BP101, BP122 to BP101, BP222 to BP101, BP480 to BP101, BP347 to BP101, BP434 to BP101, BP118 to BP101, BP137 to BP101, BP395 to BP101, BP548 to BP101, BP199 to BP101, BP542 to BP101, BP293 to BP101, BP591 to BP101, BP339 to BP101, BP136 to BP101, BP177 to BP101, BP272 to BP101, BP357 to BP101, BP298 to BP101, BP462 to BP101, BP567 to BP101, BP230 to BP101, BP443 to BP101, BP267 to BP101, BP377 to BP101, BP304 to BP101, BP590 to BP101, BP105 to BP101, BP614 to BP101, BP572 to BP101, BP501 to BP101, BP141 to BP101, BP444 to BP101, BP163 to BP101, BP108 to BP101, BP507 to BP101, BP112 to BP101, BP610 to BP101, BP354 to BP101, BP364 to BP101, BP595 to BP101, BP236 to BP101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
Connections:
- BP101 pad 1: (no net) -> GND (x354)

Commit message: Breakout Board
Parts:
- removed IO201, IO202, IO203: TestPoint, TestPoint:TestPoint_Pad_D1.0mm
- moved R101 63.5 mm to (145.7, 44.7), turned to 90 degrees
- moved D101 61.7 mm to (144.9, 42.4), turned to 180 degrees
- moved R210 61.7 mm to (66.0, 67.5)
- moved R209 61.7 mm to (66.0, 64.5)
- moved Y201 53.4 mm to (139.2, 40.5), turned to 90 degrees
- moved C205 52.6 mm to (139.1, 37.8), turned to 0 degrees
- moved C210 50.2 mm to (136.9, 41.3), turned to -90 degrees
- moved C211 49.6 mm to (136.9, 38.4), turned to 90 degrees
- moved R208 49.1 mm to (136.3, 39.9), turned to 0 degrees
- moved C208 48.1 mm to (135.8, 37.8), turned to -90 degrees
- moved C207 47.5 mm to (135.5, 36.1), turned to 0 degrees
- moved C209 45.0 mm to (132.3, 44.8), turned to 0 degrees
- moved C215 41.8 mm to (132.3, 35.3)
- moved U201 41.3 mm to (130.7, 40.0), turned to 90 degrees
- moved C216 36.9 mm to (124.7, 44.3)
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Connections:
- U201 pad 11: modbus_addr_7 -> unconnected-(U201-GPIO8-Pad11)
- U201 pad 12: modbus_addr_6 -> unconnected-(U201-GPIO9-Pad12)
- U201 pad 13: modbus_addr_5 -> unconnected-(U201-GPIO10-Pad13)
- U201 pad 14: modbus_addr_4 -> unconnected-(U201-GPIO11-Pad14)
- U201 pad 15: modbus_addr_3 -> unconnected-(U201-GPIO12-Pad15)
- U201 pad 16: modbus_addr_2 -> unconnected-(U201-GPIO13-Pad16)
- U201 pad 17: modbus_addr_1 -> unconnected-(U201-GPIO14-Pad17)
- U201 pad 18: modbus_addr_0 -> unconnected-(U201-GPIO15-Pad18)
- U201 pad 29: Net-(U201-GPIO18) -> unconnected-(U201-GPIO18-Pad29)
- U201 pad 30: Net-(U201-GPIO19) -> unconnected-(U201-GPIO19-Pad30)
- U201 pad 31: Net-(U201-GPIO20) -> unconnected-(U201-GPIO20-Pad31)
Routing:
- net button: track 22.9 -> 1.01 mm, vias 2 -> 1
- net /cpu/USB_D+: track 23.0 -> 34.8 mm
- net +3V3: track 92.3 -> 104.1 mm
- net /cpu/USB_D-: track 22.1 -> 31.7 mm
- net /cpu/QSPI_SD0: track 4.73 -> 12.2 mm, vias 0 -> 2
- net Net-(U201-GPIO18): track 7.25 -> 0.00 mm
- net Net-(U201-GPIO19): track 5.87 -> 0.00 mm
- net /cpu/QSPI_SCLK: track 6.54 -> 11.4 mm, vias 0 -> 2
- net Net-(U201-GPIO20): track 4.27 -> 0.00 mm
- net /cpu/QSPI_SD3: track 8.18 -> 12.3 mm
- net /cpu/QSPI_SS: track 18.6 -> 15.1 mm
- net /cpu/QSPI_SD1: track 14.3 -> 10.9 mm
- net GND: track 50.6 -> 48.0 mm, vias 19 -> 18
- net Net-(J203-Pin_2): track 0.00 -> 1.66 mm
- net /cpu/QSPI_SD2: track 10.3 -> 9.22 mm
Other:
- board text added: "Serial"
- board text added: "Tags"
